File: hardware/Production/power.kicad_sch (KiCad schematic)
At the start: 14 parts, among them U204 TPS62177DQCR

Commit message: Production board: tail slots, 1N/4P Kelvin nets, carrier peg holes, cup keep-outs
Schematic (make_production.py, regenerated):
- J108-J112 become plated slots for the nickel tails; J115 (1N) and J116 (4P)
  are the Kelvin fingers on new nets CELL_1N / CELL_4P (SLUA660 2.3-2.4).
  CELL_1N: gauge VSS star, U102 VSS, decoupling, NTC returns. CELL_4P: VC4,
  U102 V4/VDD, D101. Shunt, SRP and Q104 stay on CELL_N; F102 on CELL_P_RAW.
- H101-H104: cover standoffs -> 2.2 mm NPTH carrier peg holes.
- R413/R513 11.8k and the ICHG heading now come from the generator.
- Symbol uuids are kept across regens so Update PCB keeps placed parts.
- check_netlist accepts "new NAME" net moves; tidy notes updated.

Board: cup keep-outs (rails split at the filler, gap filler, tail runs,
vent, antenna, top stops), footprints swapped and nets applied from the
schematic (checked pad by pad), slots and pegs placed and locked.

make_board.py: --keepouts writes zones as text (KiCad 10 python can't build
outlines), --mech replaces --standoffs and keeps the .kicad_pro.
monolith_shell.py holds the cup's board-facing values (CUP_*, cup_rails).
Docs: README sections, p0-assembly solder order and Kelvin wording.

Co-Authored-By: Claude Opus 5.5 <noreply@anthropic.com>
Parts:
- H101, H102, H103, H104: value WA-SMSI M2 3.5mm -> Peg hole 2.2 NPTH; footprint Mounting_Wuerth:Mounting_Wuerth_WA-SMSI-M2_H3.5mm_9774035243 -> MonolithDev:Peg_NPTH_D2.2mm; symbol Mechanical:MountingHole_Pad -> Mechanical:MountingHole; LCSC C5266183 -> (none); MPN Wurth 9774035243R -> (none); now left out of the parts list
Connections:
- no-connect marks 5 -> 1
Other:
- note added: "CARRIER PEG HOLES (4x 2.2 mm NPTH for the cup carrier's 2 mm pegs; positions from mechanical/monolith_shell.py CUP_PEGS, placed by make_board.py --mech)"
- note removed: "COVER STANDOFFS (Wurth WA-SMSI M2 x 3.5 mm on F.Cu, no net; positions from mechanical/monolith_shell.py, placed by make_board.py)"
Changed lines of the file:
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@@
 		)
 	)
-	(text "NOTES\n1. PACK_P -> TPS62177 -> 3V3 (MCU + both TPS25751). Gauge BAT is NOT on this rail (TI: gauge must stay powered\n   with the FETs off).\n2. SLEEP low = sleep mode (internal 1.4 uA pull-down); CC2340 DIO21 (3V3_SLEEP) drives it, and R313 220k\n   holds it high while U301 is in reset or unprogrammed.\n3. PG is not used.\n4. U204 pin 4 (NC) goes to GND, as TI recommends.\n5. Diamonds are PWR_FLAGs (ERC only, no part): each sits where its rail is sourced through a passive part.\n6. The dev board's sleep-current section (R201 R_MEAS, 2 x INA190, HT7550-1) is not on P0: PACK_LP is PACK_P.\n   Measure sleep current on P0 with a meter in series with one pack lead (J108 or J112).\n7. C208-C213 (6 x 22u 35V 1210) = the shared battery-side bulk for both chargers and both 5 V buck inputs\n   (was one hybrid can per port). Place them between the two power stages on PACK_P, beside both RBAT pads\n   (USB sheet note 5). Nothing on the board is taller than the 3.1 mm inductors."
+	(text "NOTES\n1. PACK_P -> TPS62177 -> 3V3 (MCU + both TPS25751). Gauge BAT is NOT on this rail (TI: gauge must stay powered\n   with the FETs off).\n2. SLEEP low = sleep mode (internal 1.4 uA pull-down); CC2340 DIO21 (3V3_SLEEP) drives it, and R313 220k\n   holds it high while U301 is in reset or unprogrammed.\n3. PG is not used.\n4. U204 pin 4 (NC) goes to GND, as TI recommends.\n5. Diamonds are PWR_FLAGs (ERC only, no part): each sits where its rail is sourced through a passive part.\n6. The dev board's sleep-current section (R201 R_MEAS, 2 x INA190, HT7550-1) is not on P0: PACK_LP is PACK_P.\n   Measure sleep current on P0 with a meter in series with the PACK+ power finger (J112) before it is soldered;\n   the gauge and U102 draw through the 4P finger (J116) and are not included.\n7. C208-C213 (6 x 22u 35V 1210) = the shared battery-side bulk for both chargers and both 5 V buck inputs\n   (was one hybrid can per port). Place them between the two power stages on PACK_P, beside both RBAT pads\n   (USB sheet note 5). Nothing on the board is taller than the 3.1 mm inductors."
 		(exclude_from_sim no)
 		(at 220.98 83.82 0)
@@
 	)
 	(symbol
-		(lib_id "Mechanical:MountingHole_Pad")
+		(lib_id "Mechanical:MountingHole")
 		(at 63.5 154.94 0)
 		(unit 1)
 		(body_style 1)
 		(exclude_from_sim no)
-		(in_bom yes)
+		(in_bom no)
 		(on_board yes)
 		(in_pos_files yes)
 		(dnp no)
 		(property "Reference" "H101"
-			(at 63.50 148.65 0)
-			(show_name no)
-			(do_not_autoplace no)
-			(effects
-				(font
-					(size 1.27 1.27)
-				)
-			)
-		)
-		(property "Value" "WA-SMSI M2 3.5mm"
-			(at 63.50 150.62 0)
-			(show_name no)
-			(do_not_autoplace no)
-			(effects
-				(font
-					(size 1.27 1.27)
-				)
-			)
-		)
-		(property "Footprint" "Mounting_Wuerth:Mounting_Wuerth_WA-SMSI-M2_H3.5mm_9774035243"
+			(at 63.50 149.92 0)
+			(show_name no)
+			(do_not_autoplace no)
+			(effects
+				(font
+					(size 1.27 1.27)
+				)
+			)
+		)
+		(property "Value" "Peg hole 2.2 NPTH"
+			(at 63.50 151.89 0)
+			(show_name no)
+			(do_not_autoplace no)
+			(effects
+				(font
+					(size 1.27 1.27)
+				)
+			)
+		)
+		(property "Footprint" "MonolithDev:Peg_NPTH_D2.2mm"
 			(at 64.47 151.13 0)
 			(hide yes)
@@
 			)
 		)
-		(property "Datasheet" "https://www.we-online.com/components/products/datasheet/9774035243R.pdf"
+		(property "Datasheet" ""
 			(at 63.5 154.94 0)
 			(hide yes)
@@
 			)
 		)
-		(property "Description" "SMT steel spacer, M2 internal thread, 3.5 mm: cover standoff (mechanical/monolith_shell.py SB_STANDOFFS)"
+		(property "Description" "NPTH for a 2 mm PA12 carrier peg (mechanical/monolith_shell.py CUP_PEGS)"
 			(at 63.5 154.94 0)
 			(hide yes)
@@
 			)
 		)
-		(property "LCSC" "C5266183"
+		(property "LCSC" ""
 			(at 63.5 154.94 0)
 			(hide yes)
@@
 			)
 		)
-		(property "MPN" "Wurth 9774035243R"
+		(property "MPN" ""
 			(at 63.5 154.94 0)
 			(hide yes)
@@
 				)
 			)
-		)
-		(pin "1"
 		)
 		(instances
@@
 	)
 	(symbol
-		(lib_id "Mechanical:MountingHole_Pad")
+		(lib_id "Mechanical:MountingHole")
 		(at 78.74 154.94 0)
 		(unit 1)
 		(body_style 1)
 		(exclude_from_sim no)
-		(in_bom yes)
+		(in_bom no)
 		(on_board yes)
 		(in_pos_files yes)
 		(dnp no)
 		(property "Reference" "H102"
-			(at 78.74 159.26 0)
-			(show_name no)
-			(do_not_autoplace no)
-			(effects
-				(font
-					(size 1.27 1.27)
-				)
-			)
-		)
-		(property "Value" "WA-SMSI M2 3.5mm"
-			(at 78.74 161.23 0)
-			(show_name no)
-			(do_not_autoplace no)
-			(effects
-				(font
-					(size 1.27 1.27)
-				)
-			)
-		)
-		(property "Footprint" "Mounting_Wuerth:Mounting_Wuerth_WA-SMSI-M2_H3.5mm_9774035243"
+			(at 78.74 157.99 0)
+			(show_name no)
+			(do_not_autoplace no)
+			(effects
+				(font
+					(size 1.27 1.27)
+				)
+			)
+		)
+		(property "Value" "Peg hole 2.2 NPTH"
+			(at 78.74 159.96 0)
+			(show_name no)
+			(do_not_autoplace no)
+			(effects
+				(font
+					(size 1.27 1.27)
+				)
+			)
+		)
+		(property "Footprint" "MonolithDev:Peg_NPTH_D2.2mm"
 			(at 79.7 151.13 0)
 			(hide yes)
@@
 			)
 		)
-		(property "Datasheet" "https://www.we-online.com/components/products/datasheet/9774035243R.pdf"
+		(property "Datasheet" ""
 			(at 78.74 154.94 0)
 			(hide yes)
@@
 			)
 		)
-		(property "Description" "SMT steel spacer, M2 internal thread, 3.5 mm: cover standoff (mechanical/monolith_shell.py SB_STANDOFFS)"
+		(property "Description" "NPTH for a 2 mm PA12 carrier peg (mechanical/monolith_shell.py CUP_PEGS)"
 			(at 78.74 154.94 0)
 			(hide yes)
@@
 			)
 		)
-		(property "LCSC" "C5266183"
+		(property "LCSC" ""
 			(at 78.74 154.94 0)
 			(hide yes)
@@
 			)
 		)
-		(property "MPN" "Wurth 9774035243R"
+		(property "MPN" ""
 			(at 78.74 154.94 0)
 			(hide yes)
@@
 				)
 			)
-		)
-		(pin "1"
 		)
 		(instances
@@
 	)
 	(symbol
-		(lib_id "Mechanical:MountingHole_Pad")
+		(lib_id "Mechanical:MountingHole")
 		(at 93.98 154.94 0)
 		(unit 1)
 		(body_style 1)
 		(exclude_from_sim no)
-		(in_bom yes)
+		(in_bom no)
 		(on_board yes)
 		(in_pos_files yes)
 		(dnp no)
 		(property "Reference" "H103"
-			(at 93.98 148.65 0)
-			(show_name no)
-			(do_not_autoplace no)
-			(effects
-				(font
-					(size 1.27 1.27)
-				)
-			)
-		)
-		(property "Value" "WA-SMSI M2 3.5mm"
-			(at 93.98 150.62 0)
-			(show_name no)
-			(do_not_autoplace no)
-			(effects
-				(font
-					(size 1.27 1.27)
-				)
-			)
-		)
-		(property "Footprint" "Mounting_Wuerth:Mounting_Wuerth_WA-SMSI-M2_H3.5mm_9774035243"
+			(at 93.98 149.92 0)
+			(show_name no)
+			(do_not_autoplace no)
+			(effects
+				(font
+					(size 1.27 1.27)
+				)
+			)
+		)
+		(property "Value" "Peg hole 2.2 NPTH"
+			(at 93.98 151.89 0)
+			(show_name no)
+			(do_not_autoplace no)
+			(effects
+				(font
+					(size 1.27 1.27)
+				)
+			)
+		)
+		(property "Footprint" "MonolithDev:Peg_NPTH_D2.2mm"
 			(at 94.95 151.13 0)
 			(hide yes)
@@
 			)
 		)
-		(property "Datasheet" "https://www.we-online.com/components/products/datasheet/9774035243R.pdf"
+		(property "Datasheet" ""
 			(at 93.98 154.94 0)
 			(hide yes)
@@
 			)
 		)
-		(property "Description" "SMT steel spacer, M2 internal thread, 3.5 mm: cover standoff (mechanical/monolith_shell.py SB_STANDOFFS)"
+		(property "Description" "NPTH for a 2 mm PA12 carrier peg (mechanical/monolith_shell.py CUP_PEGS)"
 			(at 93.98 154.94 0)
 			(hide yes)
@@
 			)
 		)
-		(property "LCSC" "C5266183"
+		(property "LCSC" ""
 			(at 93.98 154.94 0)
 			(hide yes)
@@
 			)
 		)
-		(property "MPN" "Wurth 9774035243R"
+		(property "MPN" ""
 			(at 93.98 154.94 0)
 			(hide yes)
@@
 				)
 			)
-		)
-		(pin "1"
 		)
 		(instances
@@
 	)
 	(symbol
-		(lib_id "Mechanical:MountingHole_Pad")
+		(lib_id "Mechanical:MountingHole")
 		(at 109.22 154.94 0)
 		(unit 1)
 		(body_style 1)
 		(exclude_from_sim no)
-		(in_bom yes)
+		(in_bom no)
 		(on_board yes)
 		(in_pos_files yes)
 		(dnp no)
 		(property "Reference" "H104"
-			(at 109.22 159.26 0)
-			(show_name no)
-			(do_not_autoplace no)
-			(effects
-				(font
-					(size 1.27 1.27)
-				)
-			)
-		)
-		(property "Value" "WA-SMSI M2 3.5mm"
-			(at 109.22 161.23 0)
-			(show_name no)
-			(do_not_autoplace no)
-			(effects
-				(font
-					(size 1.27 1.27)
-				)
-			)
-		)
-		(property "Footprint" "Mounting_Wuerth:Mounting_Wuerth_WA-SMSI-M2_H3.5mm_9774035243"
+			(at 109.22 157.99 0)
+			(show_name no)
+			(do_not_autoplace no)
+			(effects
+				(font
+					(size 1.27 1.27)
+				)
+			)
+		)
+		(property "Value" "Peg hole 2.2 NPTH"
+			(at 109.22 159.96 0)
+			(show_name no)
+			(do_not_autoplace no)
+			(effects
+				(font
+					(size 1.27 1.27)
+				)
+			)
+		)
+		(property "Footprint" "MonolithDev:Peg_NPTH_D2.2mm"
 			(at 110.19 151.13 0)
 			(hide yes)
@@
 			)
 		)
-		(property "Datasheet" "https://www.we-online.com/components/products/datasheet/9774035243R.pdf"
+		(property "Datasheet" ""
 			(at 109.22 154.94 0)
 			(hide yes)
@@
 			)
 		)
-		(property "Description" "SMT steel spacer, M2 internal thread, 3.5 mm: cover standoff (mechanical/monolith_shell.py SB_STANDOFFS)"
+		(property "Description" "NPTH for a 2 mm PA12 carrier peg (mechanical/monolith_shell.py CUP_PEGS)"
 			(at 109.22 154.94 0)
 			(hide yes)
@@
 			)
 		)
-		(property "LCSC" "C5266183"
+		(property "LCSC" ""
 			(at 109.22 154.94 0)
 			(hide yes)
@@
 			)
 		)
-		(property "MPN" "Wurth 9774035243R"
+		(property "MPN" ""
 			(at 109.22 154.94 0)
 			(hide yes)
@@
 				)
 			)
-		)
-		(pin "1"
 		)
 		(instances
@@
 		)
 	)
-	(no_connect
-		(at 63.5 157.48)
-	)
-	(no_connect
-		(at 78.74 157.48)
-	)
-	(no_connect
-		(at 93.98 157.48)
-	)
-	(no_connect
-		(at 109.22 157.48)
-	)
-	(text "COVER STANDOFFS  (Wurth WA-SMSI M2 x 3.5 mm on F.Cu, no net; positions from mechanical/monolith_shell.py, placed by make_board.py)"
+	(text "CARRIER PEG HOLES  (4x 2.2 mm NPTH for the cup carrier's 2 mm pegs; positions from mechanical/monolith_shell.py CUP_PEGS, placed by make_board.py --mech)"
 		(exclude_from_sim no)
 		(at 40.64 142.24 0)

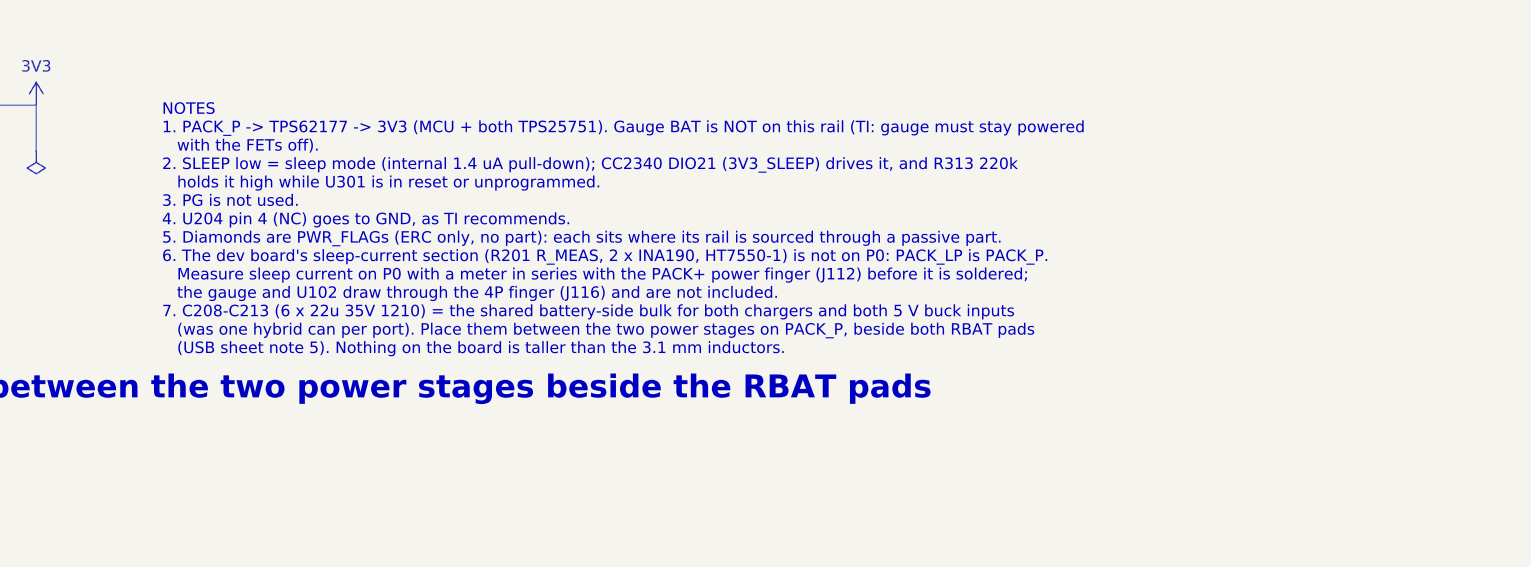
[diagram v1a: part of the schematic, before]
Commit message: Production board: PACK wire holes for the option C wire tails
J108 / J112 go from the 4.6 mm PACK power slots to Ø1.5 mm plated holes
(0.4 mm ring) for the 18 AWG thin-wall PTFE power wires, at sb_pack_holes():
KiCad (86.975, 135.7255) and (113.025, 135.7255), F.Cu, locked. The Kelvin
wires stay in the J115 / J116 slots.

- make_production.py: WIRE_FP footprint generated from SB_PWIRE_*, used for
  J108 / J112; SLOT_REFS keeps the five slots, WIRE_REFS the two holes.
- make_board.py: --mech also places the wire holes; keepout_list() follows
  the merged model (three tail runs, four KO_B_wire_* from sb_wire_runs()).
- Board: J108 / J112 swapped and placed as Update PCB + --mech would; the four
  PACK / Kelvin finger tail keep-outs replaced by KO_B_wire_*. Other
  keep-outs untouched (KO_F_above_antenna stays removed).
- Schematic Footprint / Value fields and sheet notes; Slot_Tab_4.6x0.6mm
  dropped from the library; README, spec and assembly docs.

KiCad is not available in this environment, so DRC has not been run; a
script check covers the outline, edge rule, ring and courtyards.

Co-Authored-By: Claude Opus 5.5 (1M context) <noreply@anthropic.com>
Claude-Session: https://claude.ai/code/session_01VT5ZsG8mLjRjzAJFn7LJRo
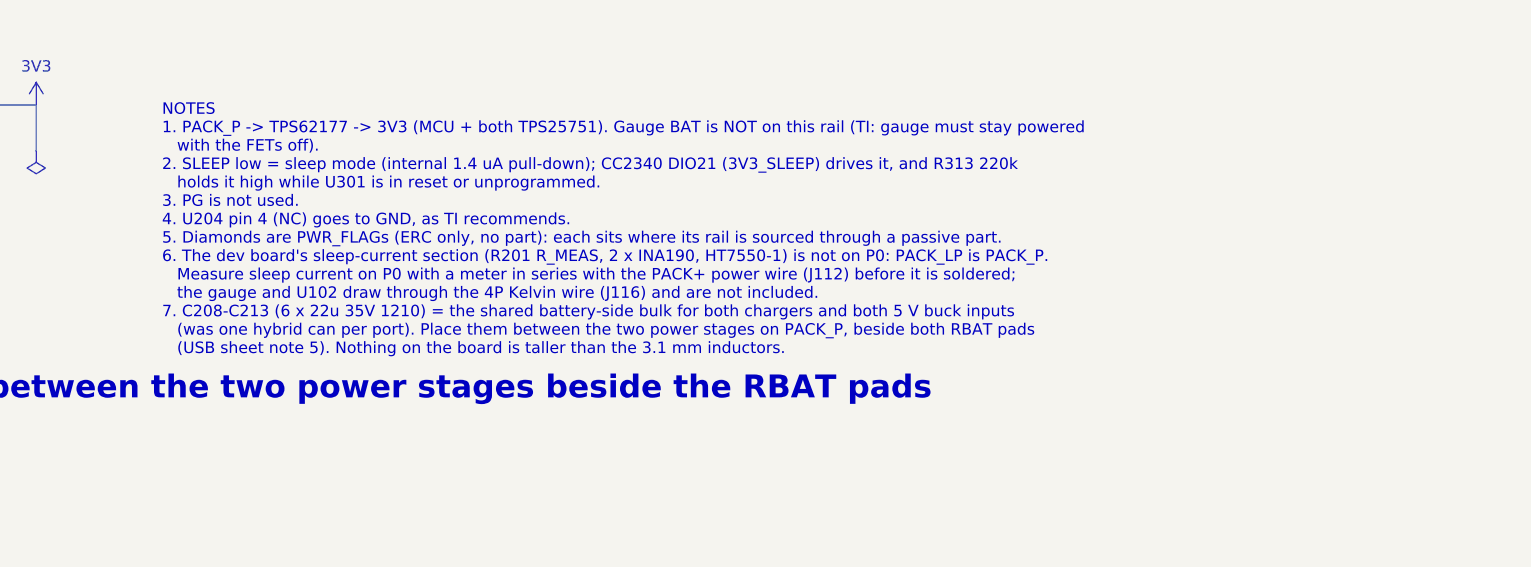
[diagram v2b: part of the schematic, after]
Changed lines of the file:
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@@
 		)
 	)
-	(text "NOTES\n1. PACK_P -> TPS62177 -> 3V3 (MCU + both TPS25751). Gauge BAT is NOT on this rail (TI: gauge must stay powered\n   with the FETs off).\n2. SLEEP low = sleep mode (internal 1.4 uA pull-down); CC2340 DIO21 (3V3_SLEEP) drives it, and R313 220k\n   holds it high while U301 is in reset or unprogrammed.\n3. PG is not used.\n4. U204 pin 4 (NC) goes to GND, as TI recommends.\n5. Diamonds are PWR_FLAGs (ERC only, no part): each sits where its rail is sourced through a passive part.\n6. The dev board's sleep-current section (R201 R_MEAS, 2 x INA190, HT7550-1) is not on P0: PACK_LP is PACK_P.\n   Measure sleep current on P0 with a meter in series with the PACK+ power finger (J112) before it is soldered;\n   the gauge and U102 draw through the 4P finger (J116) and are not included.\n7. C208-C213 (6 x 22u 35V 1210) = the shared battery-side bulk for both chargers and both 5 V buck inputs\n   (was one hybrid can per port). Place them between the two power stages on PACK_P, beside both RBAT pads\n   (USB sheet note 5). Nothing on the board is taller than the 3.1 mm inductors."
+	(text "NOTES\n1. PACK_P -> TPS62177 -> 3V3 (MCU + both TPS25751). Gauge BAT is NOT on this rail (TI: gauge must stay powered\n   with the FETs off).\n2. SLEEP low = sleep mode (internal 1.4 uA pull-down); CC2340 DIO21 (3V3_SLEEP) drives it, and R313 220k\n   holds it high while U301 is in reset or unprogrammed.\n3. PG is not used.\n4. U204 pin 4 (NC) goes to GND, as TI recommends.\n5. Diamonds are PWR_FLAGs (ERC only, no part): each sits where its rail is sourced through a passive part.\n6. The dev board's sleep-current section (R201 R_MEAS, 2 x INA190, HT7550-1) is not on P0: PACK_LP is PACK_P.\n   Measure sleep current on P0 with a meter in series with the PACK+ power wire (J112) before it is soldered;\n   the gauge and U102 draw through the 4P Kelvin wire (J116) and are not included.\n7. C208-C213 (6 x 22u 35V 1210) = the shared battery-side bulk for both chargers and both 5 V buck inputs\n   (was one hybrid can per port). Place them between the two power stages on PACK_P, beside both RBAT pads\n   (USB sheet note 5). Nothing on the board is taller than the 3.1 mm inductors."
 		(exclude_from_sim no)
 		(at 220.98 83.82 0)

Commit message: Peg holes to 2.6 x 2.2 slots so the USB-C seal bores centre the ports
The four carrier peg holes (H101-H104) were Ø2.2 for Ø2.0 pegs, so the
pegs, not the seal bores, set where the USB-C rings sit. They are now
2.6 x 2.2 NPTH slots, long across the board: +-0.3 float in y lets the
bores' 0.3 lead-in centre the rings along their long side, and +-0.1 in
z keeps a cable push from sliding the board down and pulling the rings
out of the top wall. The Ø4 TPU sleeves still cover the slots at full
float, and the board-face wall sits 0.5 over them.

- monolith_shell: CUP_PEG_SLOT replaces CUP_PEG_HOLE_D
- monolith_cup: checks for the float, ring depth and sleeve cover
- make_production: peg_footprint() draws the slot; new library footprint
  Peg_NPTH_Slot2.6x2.2mm, old D2.2 removed; board copies and schematic
  fields match it
- docs: p0-assembly and README; flags U405 pins 2.0 mm from H104 (the
  sleeve lands on them, and the bigger courtyard overlaps U405's)

Co-Authored-By: Claude Opus 5.5 (1M context) <noreply@anthropic.com>
Claude-Session: https://claude.ai/code/session_01V2XuchjL8SPbkwDuzZLoSy
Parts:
- H101, H102, H103, H104: value Peg hole 2.2 NPTH -> Peg slot 2.6x2.2 NPTH; footprint MonolithDev:Peg_NPTH_D2.2mm -> MonolithDev:Peg_NPTH_Slot2.6x2.2mm
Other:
- note added: "CARRIER PEG SLOTS (4x 2.6 x 2.2 mm NPTH for the cup carrier's 2 mm pegs; positions from mechanical/monolith_shell.py CUP_PEGS, placed by make_board.py --mech)"
- note removed: "CARRIER PEG HOLES (4x 2.2 mm NPTH for the cup carrier's 2 mm pegs; positions from mechanical/monolith_shell.py CUP_PEGS, placed by make_board.py --mech)"
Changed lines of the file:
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@@
 			)
 		)
-		(property "Value" "Peg hole 2.2 NPTH"
+		(property "Value" "Peg slot 2.6x2.2 NPTH"
 			(at 63.50 151.89 0)
 			(show_name no)
@@
 			)
 		)
-		(property "Footprint" "MonolithDev:Peg_NPTH_D2.2mm"
+		(property "Footprint" "MonolithDev:Peg_NPTH_Slot2.6x2.2mm"
 			(at 64.47 151.13 0)
 			(hide yes)
@@
 			)
 		)
-		(property "Value" "Peg hole 2.2 NPTH"
+		(property "Value" "Peg slot 2.6x2.2 NPTH"
 			(at 78.74 159.96 0)
 			(show_name no)
@@
 			)
 		)
-		(property "Footprint" "MonolithDev:Peg_NPTH_D2.2mm"
+		(property "Footprint" "MonolithDev:Peg_NPTH_Slot2.6x2.2mm"
 			(at 79.7 151.13 0)
 			(hide yes)
@@
 			)
 		)
-		(property "Value" "Peg hole 2.2 NPTH"
+		(property "Value" "Peg slot 2.6x2.2 NPTH"
 			(at 93.98 151.89 0)
 			(show_name no)
@@
 			)
 		)
-		(property "Footprint" "MonolithDev:Peg_NPTH_D2.2mm"
+		(property "Footprint" "MonolithDev:Peg_NPTH_Slot2.6x2.2mm"
 			(at 94.95 151.13 0)
 			(hide yes)
@@
 			)
 		)
-		(property "Value" "Peg hole 2.2 NPTH"
+		(property "Value" "Peg slot 2.6x2.2 NPTH"
 			(at 109.22 159.96 0)
 			(show_name no)
@@
 			)
 		)
-		(property "Footprint" "MonolithDev:Peg_NPTH_D2.2mm"
+		(property "Footprint" "MonolithDev:Peg_NPTH_Slot2.6x2.2mm"
 			(at 110.19 151.13 0)
 			(hide yes)
@@
 		)
 	)
-	(text "CARRIER PEG HOLES  (4x 2.2 mm NPTH for the cup carrier's 2 mm pegs; positions from mechanical/monolith_shell.py CUP_PEGS, placed by make_board.py --mech)"
+	(text "CARRIER PEG SLOTS  (4x 2.6 x 2.2 mm NPTH for the cup carrier's 2 mm pegs; positions from mechanical/monolith_shell.py CUP_PEGS, placed by make_board.py --mech)"
 		(exclude_from_sim no)
 		(at 40.64 142.24 0)
